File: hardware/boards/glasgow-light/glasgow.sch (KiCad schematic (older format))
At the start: 85 parts, among them J1 USB_C_USB2.0, U15 TPD3S014, U36 TLV73312PQDRVR, U5 ICE40UP5K-SG48ITR, U7 GD32VF103, U8 TLV75533PDRVR, Y1 8M

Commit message: open project on another host
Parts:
- J1: symbol Connector:USB_C_Receptacle_USB2.0 -> glasgow-rescue:USB_C_Receptacle_USB2.0-Connector
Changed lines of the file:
@@
 EESchema Schematic File Version 4
-EELAYER 30 0
+LIBS:glasgow-cache
+EELAYER 29 0
 EELAYER END
 $Descr A4 11693 8268
@@
 NoConn ~ 1500 5550
 $Comp
-L Connector:USB_C_Receptacle_USB2.0 J1
+L glasgow-rescue:USB_C_Receptacle_USB2.0-Connector J1
 U 1 1 5ED2E76F
 P 900 4950

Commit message: add GD32VF103T in QFN36 package
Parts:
- added U? (x4): GD32VF103T, Package_DFN_QFN:QFN-36-1EP_6x6mm_P0.5mm_EP4.1x4.1mm, symbol Glasgow:GD32VF103T
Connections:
- net labels added: BOOT0, NRST, VDDA
- wire segments 340 -> 381
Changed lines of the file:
@@
 Text Label 4800 -4650 2    50   ~ 0
 FPGA_DONE
+$Comp
+L Glasgow:GD32VF103T U?
+U 1 1 603FF9FD
+P 6900 -6200
+F 0 "U?" H 6842 -5435 50  0000 C CNN
+F 1 "GD32VF103T" H 6842 -5526 50  0000 C CNN
+F 2 "Package_DFN_QFN:QFN-36-1EP_6x6mm_P0.5mm_EP4.1x4.1mm" H 6900 -6200 50  0001 C CNN
+F 3 "http://www.gd32mcu.com/data/documents/shujushouce/GD32VF103_Datasheet_Rev_1.3.pdf" H 6900 -6200 50  0001 C CNN
+	1    6900 -6200
+	-1   0    0    -1
+$EndComp
+$Comp
+L Glasgow:GD32VF103T U?
+U 2 1 6040456B
+P 6900 -4600
+F 0 "U?" H 6842 -3835 50  0000 C CNN
+F 1 "GD32VF103T" H 6842 -3926 50  0000 C CNN
+F 2 "Package_DFN_QFN:QFN-36-1EP_6x6mm_P0.5mm_EP4.1x4.1mm" H 6900 -4600 50  0001 C CNN
+F 3 "http://www.gd32mcu.com/data/documents/shujushouce/GD32VF103_Datasheet_Rev_1.3.pdf" H 6900 -4600 50  0001 C CNN
+	2    6900 -4600
+	-1   0    0    -1
+$EndComp
+$Comp
+L Glasgow:GD32VF103T U?
+U 3 1 604078AB
+P 6850 -3000
+F 0 "U?" H 6767 -2135 50  0000 C CNN
+F 1 "GD32VF103T" H 6767 -2226 50  0000 C CNN
+F 2 "Package_DFN_QFN:QFN-36-1EP_6x6mm_P0.5mm_EP4.1x4.1mm" H 6850 -3000 50  0001 C CNN
+F 3 "http://www.gd32mcu.com/data/documents/shujushouce/GD32VF103_Datasheet_Rev_1.3.pdf" H 6850 -3000 50  0001 C CNN
+	3    6850 -3000
+	-1   0    0    -1
+$EndComp
+$Comp
+L Glasgow:GD32VF103T U?
+U 4 1 60409FF5
+P 6950 -1350
+F 0 "U?" H 6900 -485 50  0000 C CNN
+F 1 "GD32VF103T" H 6900 -576 50  0000 C CNN
+F 2 "Package_DFN_QFN:QFN-36-1EP_6x6mm_P0.5mm_EP4.1x4.1mm" H 6950 -1350 50  0001 C CNN
+F 3 "http://www.gd32mcu.com/data/documents/shujushouce/GD32VF103_Datasheet_Rev_1.3.pdf" H 6950 -1350 50  0001 C CNN
+	4    6950 -1350
+	1    0    0    -1
+$EndComp
+Text Label 7550 -2550 2    50   ~ 0
+SDA
+Text Label 7550 -2700 2    50   ~ 0
+SCL
+Wire Wire Line
+	7300 -4200 7550 -4200
+Text Label 7350 -4200 0    50   ~ 0
+USB_N
+Wire Wire Line
+	7300 -4050 7550 -4050
+Text Label 7350 -4050 0    50   ~ 0
+USB_P
+Wire Wire Line
+	7300 -4500 7550 -4500
+$Comp
+L power:+5V #PWR?
+U 1 1 6040CC09
+P 7550 -4500
+F 0 "#PWR?" H 7550 -4650 50  0001 C CNN
+F 1 "+5V" H 7400 -4450 50  0000 C CNN
+F 2 "" H 7550 -4500 50  0001 C CNN
+F 3 "" H 7550 -4500 50  0001 C CNN
+	1    7550 -4500
+	0    1    1    0
+$EndComp
+Text GLabel 7400 -6700 2    50   Input ~ 0
+ADC0
+Text GLabel 7400 -6550 2    50   Input ~ 0
+ADC1
+Text GLabel 7400 -6400 2    50   Input ~ 0
+ADC2
+Text GLabel 7400 -6250 2    50   Input ~ 0
+ADC3
+Text GLabel 7400 -5800 2    50   Input ~ 0
+ADC4
+Text GLabel 7400 -5650 2    50   Input ~ 0
+ADC5
+Text GLabel 7450 -4950 2    50   Input ~ 0
+VIO_CURRENT
+Text GLabel 7450 -5100 2    50   Input ~ 0
+ADC6
+Text GLabel 7450 -3300 2    50   Input ~ 0
+FPGA_CS
+Text GLabel 7450 -3150 2    50   Input ~ 0
+FPGA_SCK
+Text GLabel 7450 -3000 2    50   Input ~ 0
+FPGA_MISO
+Text GLabel 7450 -2850 2    50   Input ~ 0
+FPGA_MOSI
+Text Label 7650 -4350 2    50   ~ 0
+LED_ACT
+Wire Wire Line
+	7300 -4650 8000 -4650
+Wire Wire Line
+	7450 -2850 7300 -2850
+Wire Wire Line
+	7300 -3000 7450 -3000
+Wire Wire Line
+	7450 -3150 7300 -3150
+Wire Wire Line
+	7300 -3300 7450 -3300
+Wire Wire Line
+	7300 -4950 7450 -4950
+Wire Wire Line
+	7300 -5100 7450 -5100
+Text GLabel 7450 -4800 2    50   Input ~ 0
+VIO_ENA
+Text Notes 7900 -4750 0    50   ~ 0
+PB2 is also BOOT1, which should be low during startup
+Wire Wire Line
+	7400 -5650 7300 -5650
+Wire Wire Line
+	7300 -5800 7400 -5800
+Wire Wire Line
+	7300 -6250 7400 -6250
+Wire Wire Line
+	7300 -6400 7400 -6400
+Wire Wire Line
+	7300 -6550 7400 -6550
+Wire Wire Line
+	7300 -6700 7400 -6700
+Text GLabel 7400 -5950 2    50   Input ~ 0
+ADC7
+Wire Wire Line
+	7400 -5950 7300 -5950
+Wire Wire Line
+	7300 -6100 7400 -6100
+Text GLabel 7400 -6100 2    50   Input ~ 0
+VIO_DAC
+Text Label 8000 -4650 2    50   ~ 0
+CLKREF
+Wire Wire Line
+	7300 -4350 7650 -4350
+Wire Wire Line
+	7300 -4800 7450 -4800
+Text Label 4400 -3500 1    50   ~ 0
+VDDA
+Text Label 7650 -1950 2    50   ~ 0
+VDDA
+Wire Wire Line
+	7650 -1950 7350 -1950
+Text Label 6100 -1500 0    50   ~ 0
+XTALOUT
+Text Label 6100 -1350 0    50   ~ 0
+XTALIN
+Wire Wire Line
+	6100 -1350 6450 -1350
+Wire Wire Line
+	6450 -1500 6100 -1500
+Text Label 3250 -2600 0    50   ~ 0
+NRST
+Text Label 6100 -1200 0    50   ~ 0
+NRST
+Wire Wire Line
+	6100 -1200 6450 -1200
+$Comp
+L power:GND #PWR?
+U 1 1 605BF48B
+P 7500 -900
+F 0 "#PWR?" H 7500 -1150 50  0001 C CNN
+F 1 "GND" H 7505 -1073 50  0000 C CNN
+F 2 "" H 7500 -900 50  0001 C CNN
+F 3 "" H 7500 -900 50  0001 C CNN
+	1    7500 -900
+	0    -1   -1   0
+$EndComp
+$Comp
+L power:+3.3V #PWR?
+U 1 1 605BF9C6
+P 7500 -1800
+F 0 "#PWR?" H 7500 -1950 50  0001 C CNN
+F 1 "+3.3V" H 7515 -1627 50  0000 C CNN
+F 2 "" H 7500 -1800 50  0001 C CNN
+F 3 "" H 7500 -1800 50  0001 C CNN
+	1    7500 -1800
+	0    1    1    0
+$EndComp
+Wire Wire Line
+	7350 -1800 7400 -1800
+Wire Wire Line
+	7400 -1800 7400 -1650
+Wire Wire Line
+	7400 -1500 7350 -1500
+Connection ~ 7400 -1800
+Wire Wire Line
+	7400 -1800 7500 -1800
+Wire Wire Line
+	7350 -1650 7400 -1650
+Connection ~ 7400 -1650
+Wire Wire Line
+	7400 -1650 7400 -1500
+Wire Wire Line
+	7350 -1350 7400 -1350
+Wire Wire Line
+	7400 -1350 7400 -1200
+Wire Wire Line
+	7400 -900 7350 -900
+Wire Wire Line
+	7350 -1050 7400 -1050
+Connection ~ 7400 -1050
+Wire Wire Line
+	7400 -1050 7400 -900
+Wire Wire Line
+	7350 -1200 7400 -1200
+Connection ~ 7400 -1200
+Wire Wire Line
+	7400 -1200 7400 -1050
+Wire Wire Line
+	7400 -900 7500 -900
+Connection ~ 7400 -900
+Wire Wire Line
+	7550 -2550 7300 -2550
+Wire Wire Line
+	7300 -2700 7550 -2700
+Text Label 4350 -4350 0    50   ~ 0
+BOOT0
+Text Label 7600 -2400 2    50   ~ 0
+BOOT0
+Wire Wire Line
+	7600 -2400 7300 -2400
 $EndSCHEMATC

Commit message: .
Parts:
- removed C15: u1, Capacitor_SMD:C_0402_1005Metric, symbol Device:C
- removed TP21: USBGND, TestPoint:TestPoint_Pad_D1.0mm, symbol Connector:TestPoint
- removed U7: GD32VF103, Package_QFP:LQFP-48_7x7mm_P0.5mm, symbol Glasgow:GD32VF103
- added RN13: 33R, Glasgow:R_Array_Convex_4x0402, symbol Device:R_Pack04
- added TP6: SYNC, TestPoint:TestPoint_Pad_D1.0mm, symbol Connector:TestPoint
- TP40: renamed from TP6; value USBGND -> TMS
- TP41: renamed from TP7; value USBGND -> TCK
- TP42: renamed from TP18; value USBGND -> TDI
- TP43: renamed from TP20; value USBGND -> TDO
- gave numbers to parts that had none: 1
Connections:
- net labels added: TCK, TDI, TDO, TMS
- wire segments 381 -> 348
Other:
- moved on the sheet: C11, C12, C17, R1, R10, R17, R18, R2, R7, R9, TP4, TP40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

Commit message: rotate GD32 -> routing is *much* easier
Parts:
- removed C10, C5, C6, C7, C9: u1, Capacitor_SMD:C_0402_1005Metric, symbol Device:C
- removed MK1, MK2, MK3, MK4: Mounting_Hole_PAD, Glasgow:MountingHole_3.5mm_Pad_Via_CrtYd, symbol Mechanical:MountingHole_Pad
- added C15: u1, Capacitor_SMD:C_0402_1005Metric, symbol Device:C
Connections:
- wire segments 348 -> 321
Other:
- moved on the sheet: D1, R12

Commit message: replace SYNC and AUX connectors by test points
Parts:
- removed TP6: SYNC, TestPoint:TestPoint_Pad_D1.0mm, symbol Connector:TestPoint
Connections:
- net AUX2: now reaches U5.11 (IOB_20a)
- net AUX1: now reaches U5.9 (IOB_16a)
- net ~SYNC renamed ~SYNC_INT
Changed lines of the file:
@@
 F22 "DA1" I L 9150 3100 50
 F23 "DA0" I L 9150 3000 50
+F24 "~SYNC_INT" I R 9700 2400 50
+F25 "AUX1" I R 9700 2500 50
+F26 "AUX2" I R 9700 2600 50
 $EndSheet
 Connection ~ 1350 3500
@@
 Connection ~ 4000 950
 Connection ~ 4000 1350
-Text Notes 9750 2700 0    50   ~ 0
+Text Notes 10150 2850 0    50   ~ 0
 Addr A Pull: 0100000
 $Comp
@@
 Text Label -2800 3050 2    50   ~ 0
 DA0
-Text Label -4750 2850 2    50   ~ 0
-~SYNC
+Text Label -4600 2850 2    50   ~ 0
+~SYNC_INT
 Text Label -2800 3250 2    50   ~ 0
 QA7
@@
 	-2750 3950 -2750 3750
 Wire Wire Line
-	-4750 2850 -5000 2850
+	-4600 2850 -5000 2850
 Text Label 9900 3000 2    50   ~ 0
 QA0
@@
 TDO
 $Comp
-L Connector:TestPoint TP6
-U 1 1 60EC92E0
-P -4750 2850
-F 0 "TP6" V -4850 2900 50  0000 L CNN
-F 1 "SYNC" V -4646 2924 50  0001 C CNN
-F 2 "TestPoint:TestPoint_Pad_D1.0mm" H -4550 2850 50  0001 C CNN
-F 3 "~" H -4550 2850 50  0001 C CNN
-	1    -4750 2850
-	0    1    1    0
-$EndComp
-$Comp
 L Device:C C15
 U 1 1 610429BC
@@
 	1    0    0    -1
 $EndComp
+Text Label 10100 2400 2    50   ~ 0
+~SYNC_INT
+Wire Wire Line
+	10100 2400 9700 2400
+Wire Wire Line
+	9700 2500 10100 2500
+Wire Wire Line
+	9700 2600 10100 2600
+Text Label 10100 2600 2    50   ~ 0
+AUX2
+Text Label 10100 2500 2    50   ~ 0
+AUX1
+Text Label -4600 2950 2    50   ~ 0
+AUX2
+Text Label -4600 2750 2    50   ~ 0
+AUX1
+Wire Wire Line
+	-4600 2950 -5000 2950
+Wire Wire Line
+	-5000 2750 -4600 2750
 $EndSCHEMATC

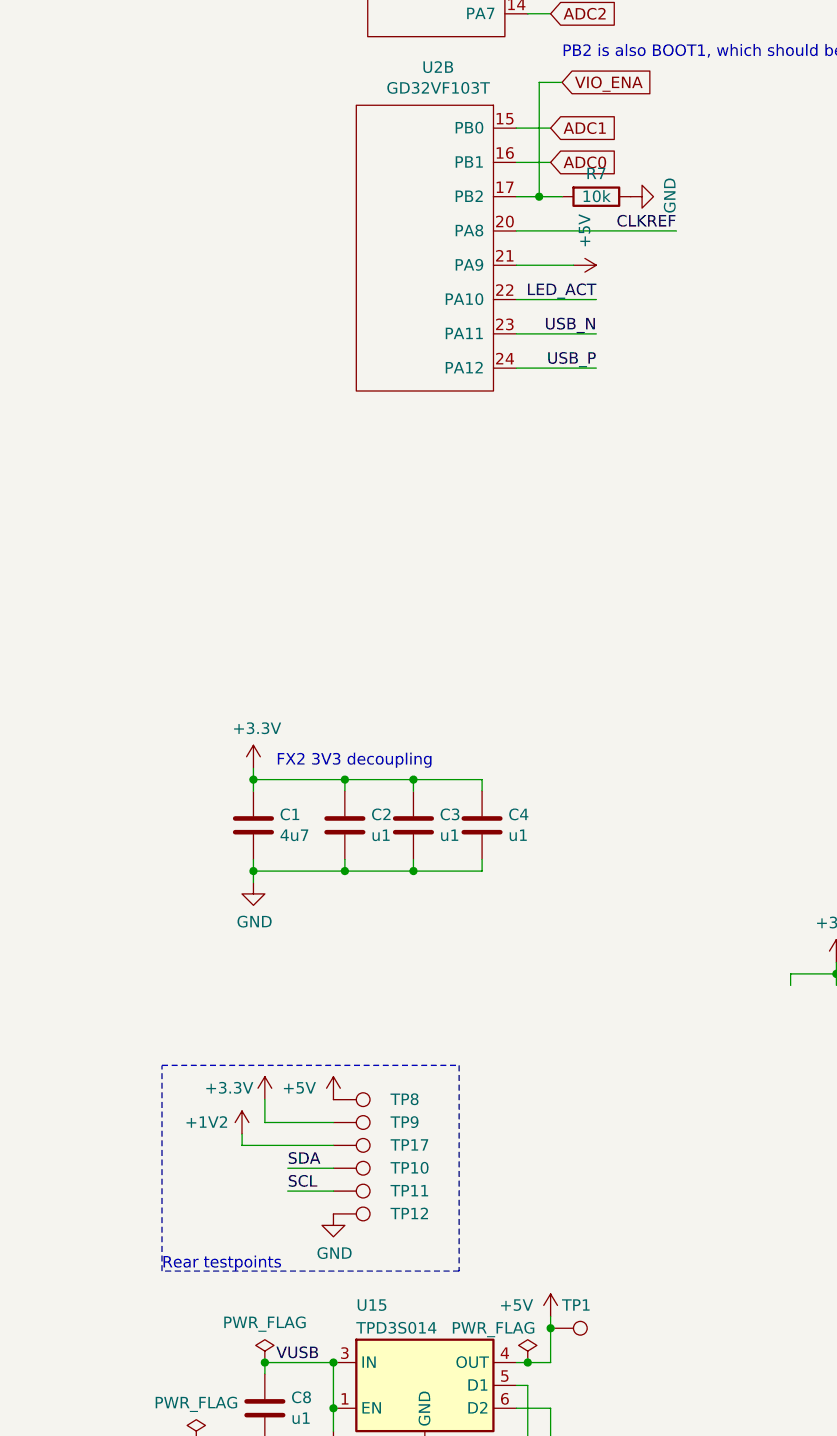
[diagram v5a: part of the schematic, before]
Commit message: most components are placed
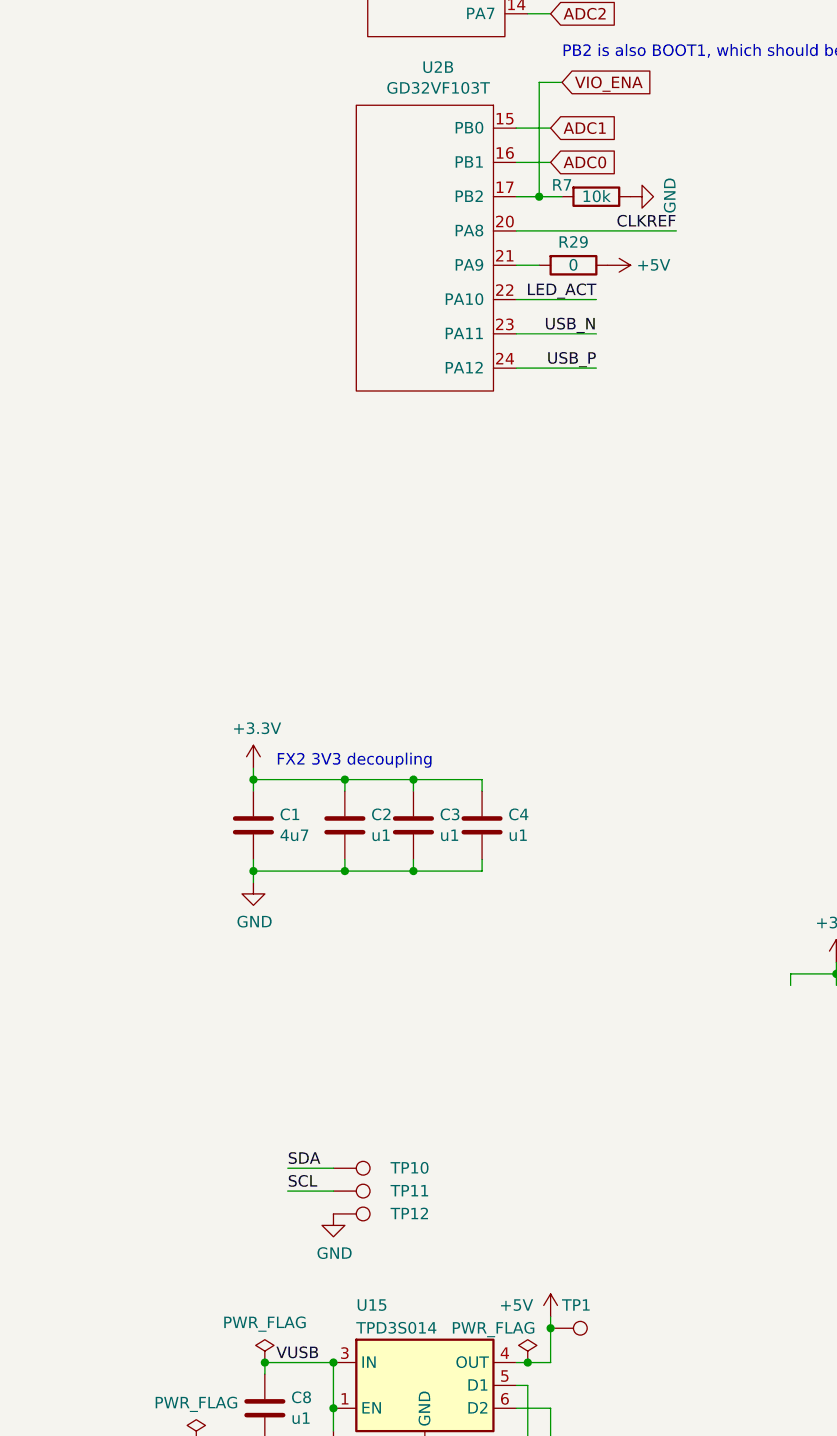
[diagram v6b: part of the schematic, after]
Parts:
- removed TP17: 1V2, TestPoint:TestPoint_Pad_D1.0mm, symbol Connector:TestPoint
- removed TP8: 5V, TestPoint:TestPoint_Pad_D1.0mm, symbol Connector:TestPoint
- removed TP9: 3V3, TestPoint:TestPoint_Pad_D1.0mm, symbol Connector:TestPoint
- added R29: 0, Resistor_SMD:R_0402_1005Metric, symbol Device:R
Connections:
- net +5V: now also R29.1; no longer U2.21 (PA9)
- new net: R29.2, U2.21 (PA9)
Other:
- note removed: "Rear testpoints"
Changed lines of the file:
@@
 CLKREF
-$Comp
-L Connector:TestPoint TP8
-U 1 1 5CA9B5FE
-P 1350 2350
-F 0 "TP8" V 1350 2600 50  0000 L CNN
-F 1 "5V" V 1454 2424 50  0001 C CNN
-F 2 "TestPoint:TestPoint_Pad_D1.0mm" H 1550 2350 50  0001 C CNN
-F 3 "~" H 1550 2350 50  0001 C CNN
-	1    1350 2350
-	0    1    1    0
-$EndComp
-$Comp
-L Connector:TestPoint TP9
-U 1 1 5CA9CCBA
-P 1350 2450
-F 0 "TP9" V 1350 2700 50  0000 L CNN
-F 1 "3V3" V 1454 2524 50  0001 C CNN
-F 2 "TestPoint:TestPoint_Pad_D1.0mm" H 1550 2450 50  0001 C CNN
-F 3 "~" H 1550 2450 50  0001 C CNN
-	1    1350 2450
-	0    1    1    0
-$EndComp
 $Comp
 L Connector:TestPoint TP10
@@
 $EndComp
 $Comp
-L power:+5V #PWR0134
-U 1 1 5CB37530
-P 1350 2350
-F 0 "#PWR0134" H 1350 2200 50  0001 C CNN
-F 1 "+5V" H 1200 2400 50  0000 C CNN
-F 2 "" H 1350 2350 50  0001 C CNN
-F 3 "" H 1350 2350 50  0001 C CNN
-	1    1350 2350
-	1    0    0    -1
-$EndComp
-$Comp
-L power:+3.3V #PWR041
-U 1 1 5CB375E7
-P 1050 2350
-F 0 "#PWR041" H 1050 2200 50  0001 C CNN
-F 1 "+3.3V" H 1000 2400 50  0000 R CNN
-F 2 "" H 1050 2350 50  0001 C CNN
-F 3 "" H 1050 2350 50  0001 C CNN
-	1    1050 2350
-	1    0    0    -1
-$EndComp
-Wire Notes Line
-	600  2200 1900 2200
-Wire Notes Line
-	1900 2200 1900 3100
-Wire Notes Line
-	1900 3100 600  3100
-Wire Notes Line
-	600  3100 600  2200
-Text Notes 600  3100 0    50   ~ 0
-Rear testpoints
-Wire Wire Line
-	1050 2350 1050 2450
-Wire Wire Line
-	1050 2450 1350 2450
-$Comp
 L power:PWR_FLAG #FLG0102
 U 1 1 5D01628B
@@
 	1    1600 4350
 	-1   0    0    1
-$EndComp
-$Comp
-L power:+1V2 #PWR0142
-U 1 1 5CC9337B
-P 950 2500
-F 0 "#PWR0142" H 950 2350 50  0001 C CNN
-F 1 "+1V2" H 1200 2550 50  0000 R CNN
-F 2 "" H 950 2500 50  0001 C CNN
-F 3 "" H 950 2500 50  0001 C CNN
-	1    950  2500
-	-1   0    0    -1
-$EndComp
-Wire Wire Line
-	950  2550 1350 2550
-Wire Wire Line
-	950  2500 950  2550
-$Comp
-L Connector:TestPoint TP17
-U 1 1 5CC2ABF8
-P 1350 2550
-F 0 "TP17" V 1350 2800 50  0000 L CNN
-F 1 "1V2" V 1454 2624 50  0001 C CNN
-F 2 "TestPoint:TestPoint_Pad_D1.0mm" H 1550 2550 50  0001 C CNN
-F 3 "~" H 1550 2550 50  0001 C CNN
-	1    1350 2550
-	0    1    1    0
 $EndComp
 $Comp
@@
 USB_P
 Wire Wire Line
-	2150 -1300 2400 -1300
+	2150 -1300 2250 -1300
 $Comp
 L power:+5V #PWR0138
 U 1 1 6196A009
-P 2400 -1300
-F 0 "#PWR0138" H 2400 -1450 50  0001 C CNN
-F 1 "+5V" H 2250 -1250 50  0000 C CNN
-F 2 "" H 2400 -1300 50  0001 C CNN
-F 3 "" H 2400 -1300 50  0001 C CNN
-	1    2400 -1300
+P 2550 -1300
+F 0 "#PWR0138" H 2550 -1450 50  0001 C CNN
+F 1 "+5V" V 2550 -1100 50  0000 C CNN
+F 2 "" H 2550 -1300 50  0001 C CNN
+F 3 "" H 2550 -1300 50  0001 C CNN
+	1    2550 -1300
 	0    1    1    0
 $EndComp
@@
 U 1 1 619754B8
 P 2500 -1600
-F 0 "R7" V 2400 -1600 50  0000 C CNN
+F 0 "R7" V 2450 -1750 50  0000 C CNN
 F 1 "10k" V 2500 -1600 50  0000 C CNN
 F 2 "Resistor_SMD:R_0402_1005Metric" V 2430 -1600 50  0001 C CNN
@@
 Wire Wire Line
 	-5000 2750 -4600 2750
+$Comp
+L Device:R R29
+U 1 1 6144C403
+P 2400 -1300
+F 0 "R29" V 2300 -1300 50  0000 C CNN
+F 1 "0" V 2400 -1300 50  0000 C CNN
+F 2 "Resistor_SMD:R_0402_1005Metric" V 2330 -1300 50  0001 C CNN
+F 3 "https://www.mouser.com/datasheet/2/447/PYu-RC_Group_51_RoHS_L_10-1527934.pdf" H 2400 -1300 50  0001 C CNN
+F 4 "Yageo" H -2000 -6600 50  0001 C CNN "Mfg"
+F 5 "RC0402FR-13100KL" H -2000 -6600 50  0001 C CNN "MPN"
+F 6 "res-0402-100k" H 2400 -1300 50  0001 C CNN "1b2-bom-key"
+	1    2400 -1300
+	0    1    1    0
+$EndComp
 $EndSCHEMATC

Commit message: optimize
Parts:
- added R11: 0, Resistor_SMD:R_0402_1005Metric, symbol Device:R
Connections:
- net GND: now also R11.2
- net at U2.37 (EP): now also R11.1
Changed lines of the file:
@@
 	0    1    1    0
 $EndComp
+$Comp
+L Device:R R11
+U 1 1 61B60DD1
+P 5950 -400
+F 0 "R11" V 5850 -400 50  0000 C CNN
+F 1 "0" V 5950 -400 50  0000 C CNN
+F 2 "Resistor_SMD:R_0402_1005Metric" V 5880 -400 50  0001 C CNN
+F 3 "https://www.mouser.com/datasheet/2/447/PYu-RC_Group_51_RoHS_L_10-1527934.pdf" H 5950 -400 50  0001 C CNN
+F 4 "Yageo" H 1550 -5700 50  0001 C CNN "Mfg"
+F 5 "RC0402FR-13100KL" H 1550 -5700 50  0001 C CNN "MPN"
+F 6 "res-0402-100k" H 5950 -400 50  0001 C CNN "1b2-bom-key"
+	1    5950 -400
+	0    -1   -1   0
+$EndComp
+Wire Wire Line
+	5800 -400 5800 -650
+$Comp
+L power:GND #PWR0115
+U 1 1 61B7F35F
+P 6100 -400
+F 0 "#PWR0115" H 6100 -650 50  0001 C CNN
+F 1 "GND" H 6105 -573 50  0000 C CNN
+F 2 "" H 6100 -400 50  0001 C CNN
+F 3 "" H 6100 -400 50  0001 C CNN
+	1    6100 -400
+	0    -1   -1   0
+$EndComp
 $EndSCHEMATC

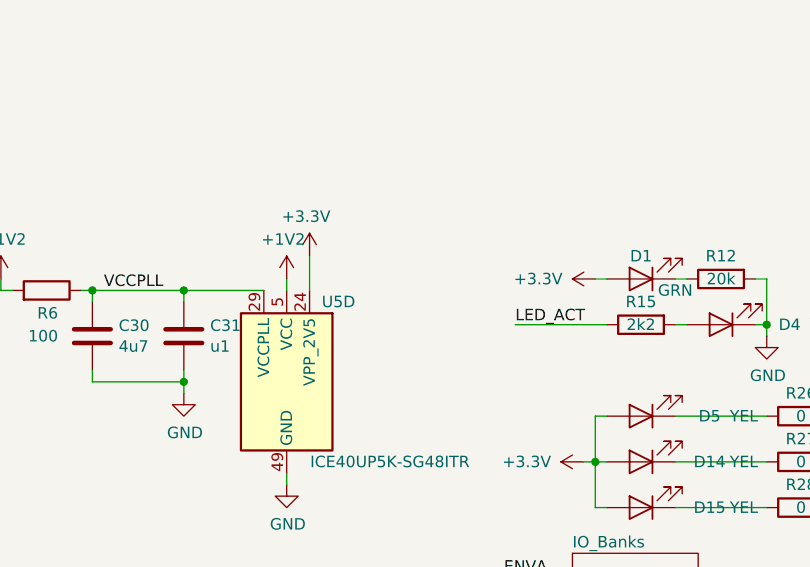
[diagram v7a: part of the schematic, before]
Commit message: add solder jumper for VPP_2V5
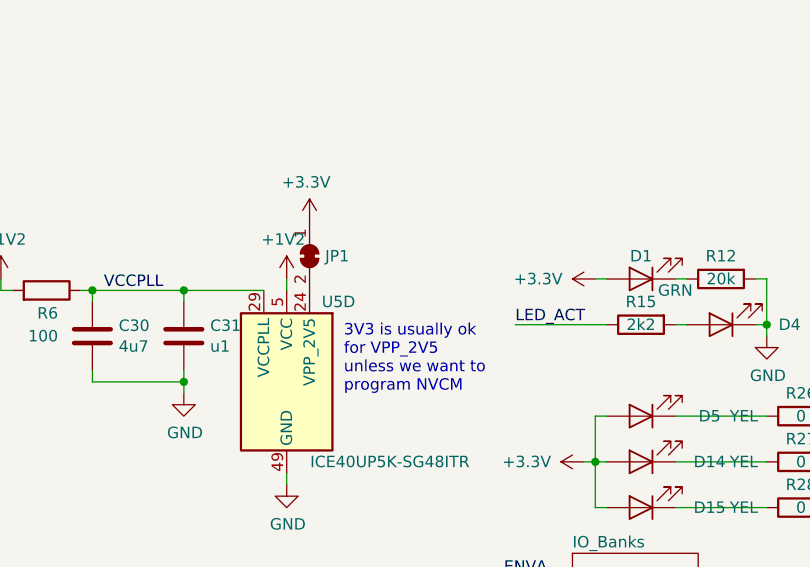
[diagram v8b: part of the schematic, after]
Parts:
- added JP1: SolderJumper_2_Bridged, Jumper:SolderJumper-2_P1.3mm_Bridged_RoundedPad1.0x1.5mm, symbol Jumper:SolderJumper_2_Bridged
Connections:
- net +3V3: now also JP1.1 (A); no longer U5.24 (VPP_2V5)
- new net: JP1.2 (B), U5.24 (VPP_2V5)
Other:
- note added: "3V3 is usually ok\nfor VPP_2V5\nunless we want to\nprogram NVCM"
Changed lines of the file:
@@
 L power:+3.3V #PWR0103
 U 1 1 5FFD4B59
-P 8000 800
-F 0 "#PWR0103" H 8000 650 50  0001 C CNN
-F 1 "+3.3V" H 8015 973 50  0000 C CNN
-F 2 "" H 8000 800 50  0001 C CNN
-F 3 "" H 8000 800 50  0001 C CNN
-	1    8000 800
+P 8000 650
+F 0 "#PWR0103" H 8000 500 50  0001 C CNN
+F 1 "+3.3V" H 8015 823 50  0000 C CNN
+F 2 "" H 8000 650 50  0001 C CNN
+F 3 "" H 8000 650 50  0001 C CNN
+	1    8000 650
 	-1   0    0    -1
 $EndComp
@@
 Wire Wire Line
 	5950 1350 6300 1350
-Wire Wire Line
-	8000 800  8000 950
 $Comp
 L power:+1V2 #PWR0114
@@
 	0    -1   -1   0
 $EndComp
+$Comp
+L Jumper:SolderJumper_2_Bridged JP1
+U 1 1 6042F790
+P 8000 800
+F 0 "JP1" V 8000 868 50  0000 L CNN
+F 1 "SolderJumper_2_Bridged" V 8045 868 50  0001 L CNN
+F 2 "Jumper:SolderJumper-2_P1.3mm_Bridged_RoundedPad1.0x1.5mm" H 8000 800 50  0001 C CNN
+F 3 "~" H 8000 800 50  0001 C CNN
+	1    8000 800
+	0    1    1    0
+$EndComp
+Text Notes 8150 1400 0    50   ~ 0
+3V3 is usually ok\nfor VPP_2V5\nunless we want to\nprogram NVCM
 $EndSCHEMATC
